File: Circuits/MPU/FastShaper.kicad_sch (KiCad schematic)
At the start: 34 parts, among them U20 ADA4805-2ARMZ, U21 ADA4805-2ARMZ

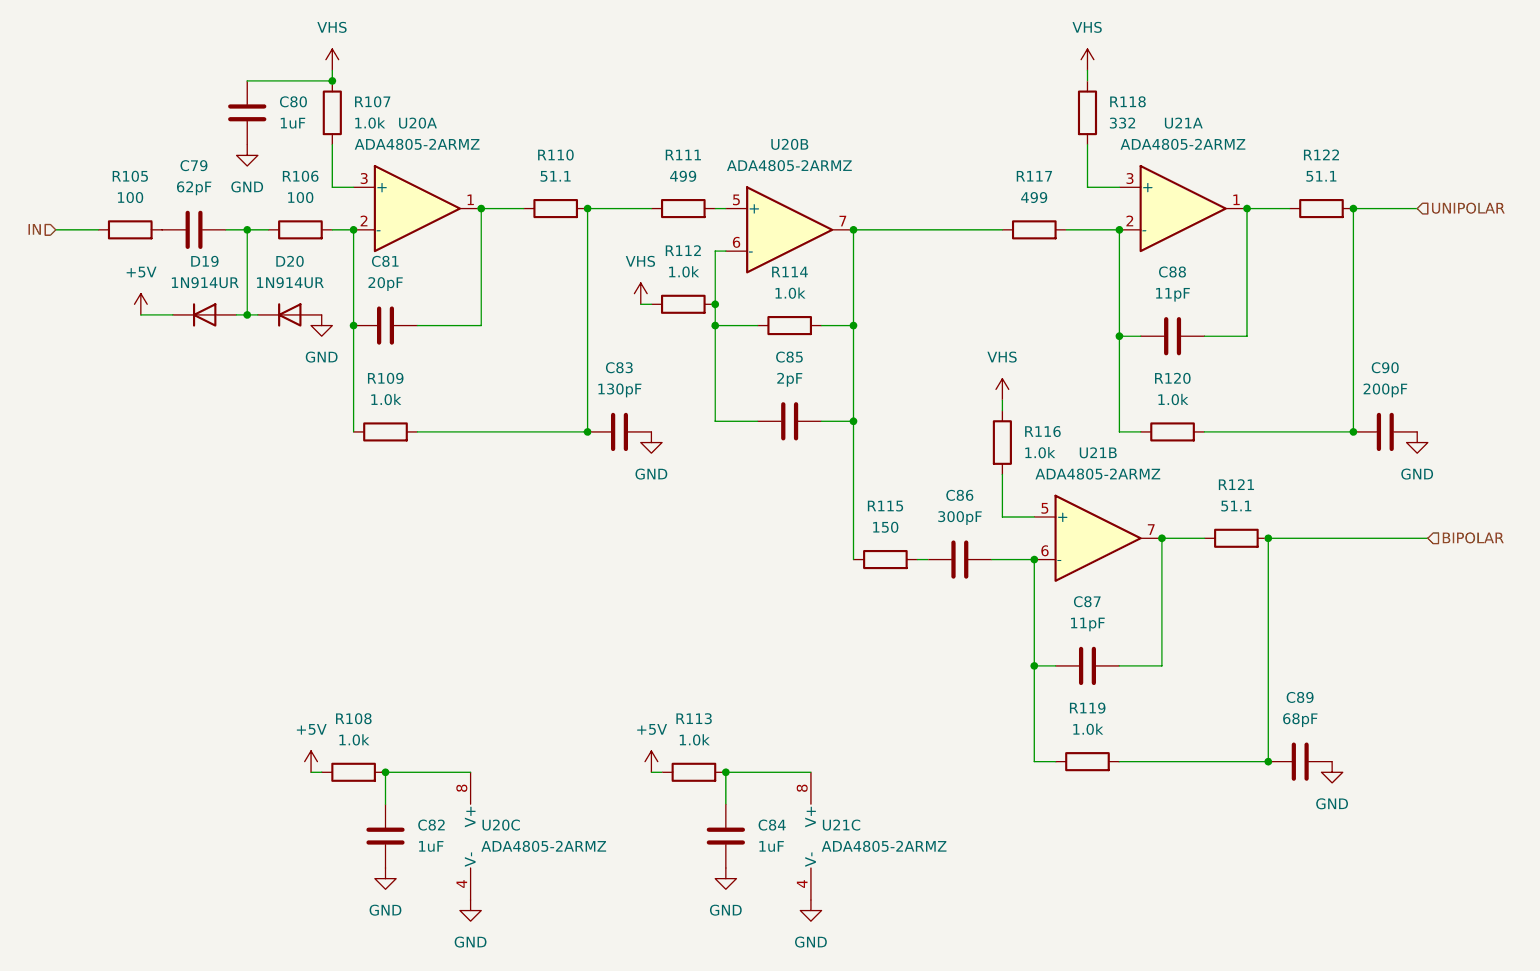
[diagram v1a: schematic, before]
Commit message: PPS is RS422, add MXINH
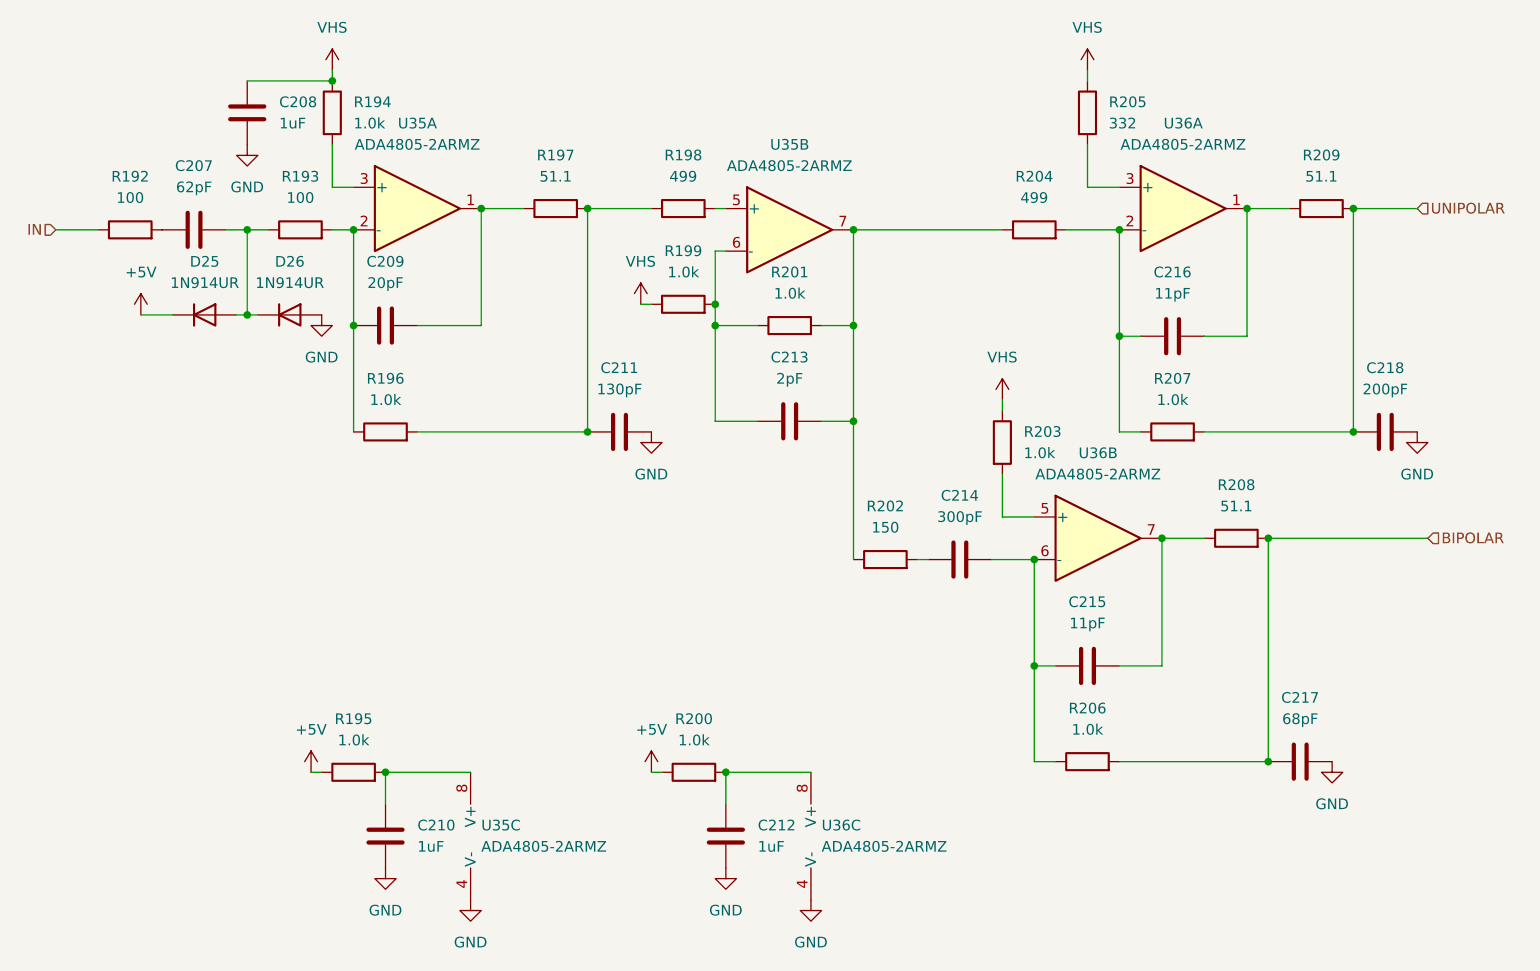
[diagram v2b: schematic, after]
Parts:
- renumbered C79 to C207, C80 to C208, C81 to C209, C82 to C210, C83 to C211, C84 to C212, C85 to C213, C86 to C214, C87 to C215, C88 to C216, C89 to C217, C90 to C218, D19 to D25, D20 to D26, R105 to R192, R106 to R193, R107 to R194, R108 to R195, R109 to R196, R110 to R197, R111 to R198, R112 to R199, R113 to R200, R114 to R201, R115 to R202, R116 to R203, R117 to R204, R118 to R205, R119 to R206, R120 to R207, R121 to R208, R122 to R209, U20 to U35, U21 to U36
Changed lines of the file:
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@@
 	(title_block
 		(title "QuERI MPU")
-		(date "2024-06-05")
-		(rev "RR1")
+		(date "2024-06-27")
+		(rev "RR3")
 		(company "Noqsi Aerospace Ltd")
 		(comment 1 "15 Blanchard Avenue, Billerica MA 01821")
@@
 		(dnp no)
 		(fields_autoplaced yes)
-		(property "Reference" "D20"
+		(property "Reference" "D26"
 			(at 69.85 72.39 0)
 			(effects
@@
 		(dnp no)
 		(fields_autoplaced yes)
-		(property "Reference" "U20"
+		(property "Reference" "U35"
 			(at 85.09 55.88 0)
 			(effects
@@
 		(dnp no)
 		(fields_autoplaced yes)
-		(property "Reference" "#PWR0191"
+		(property "Reference" "#PWR0309"
 			(at 132.08 154.94 0)
 			(effects
@@
 		(dnp no)
 		(fields_autoplaced yes)
-		(property "Reference" "#PWR0180"
+		(property "Reference" "#PWR0298"
 			(at 52.07 82.55 0)
 			(effects
@@
 		(dnp no)
 		(fields_autoplaced yes)
-		(property "Reference" "#PWR0192"
+		(property "Reference" "#PWR0310"
 			(at 154.94 92.71 0)
 			(effects
@@
 		(dnp no)
 		(fields_autoplaced yes)
-		(property "Reference" "#PWR0188"
+		(property "Reference" "#PWR0306"
 			(at 113.03 99.06 0)
 			(effects
@@
 		(dnp no)
 		(fields_autoplaced yes)
-		(property "Reference" "R117"
+		(property "Reference" "R204"
 			(at 158.75 62.23 90)
 			(effects
@@
 		(dnp no)
 		(fields_autoplaced yes)
-		(property "Reference" "#PWR0194"
+		(property "Reference" "#PWR0312"
 			(at 194.31 138.43 0)
 			(effects
@@
 		(dnp no)
 		(fields_autoplaced yes)
-		(property "Reference" "U20"
+		(property "Reference" "U35"
 			(at 92.71 139.7 0)
 			(effects
@@
 		(dnp no)
 		(fields_autoplaced yes)
-		(property "Reference" "U21"
+		(property "Reference" "U36"
 			(at 133.35 139.7 0)
 			(effects
@@
 		(dnp no)
 		(fields_autoplaced yes)
-		(property "Reference" "R120"
+		(property "Reference" "R207"
 			(at 175.26 86.36 90)
 			(effects
@@
 		(dnp no)
 		(fields_autoplaced yes)
-		(property "Reference" "C88"
+		(property "Reference" "C216"
 			(at 175.26 73.66 90)
 			(effects
@@
 		(dnp no)
 		(fields_autoplaced yes)
-		(property "Reference" "R118"
+		(property "Reference" "R205"
 			(at 167.64 53.34 0)
 			(effects
@@
 		(dnp no)
 		(fields_autoplaced yes)
-		(property "Reference" "D19"
+		(property "Reference" "D25"
 			(at 59.69 72.39 0)
 			(effects
@@
 		(dnp no)
 		(fields_autoplaced yes)
-		(property "Reference" "C84"
+		(property "Reference" "C212"
 			(at 125.73 139.7 0)
 			(effects
@@
 		(dnp no)
 		(fields_autoplaced yes)
-		(property "Reference" "R122"
+		(property "Reference" "R209"
 			(at 193.04 59.69 90)
 			(effects
@@
 		(dnp no)
 		(fields_autoplaced yes)
-		(property "Reference" "R111"
+		(property "Reference" "R198"
 			(at 116.84 59.69 90)
 			(effects
@@
 		(dnp no)
 		(fields_autoplaced yes)
-		(property "Reference" "U21"
+		(property "Reference" "U36"
 			(at 176.53 55.88 0)
 			(effects
@@
 		(dnp no)
 		(fields_autoplaced yes)
-		(property "Reference" "#PWR0185"
+		(property "Reference" "#PWR0303"
 			(at 81.28 151.13 0)
 			(effects
@@
 		(dnp no)
 		(fields_autoplaced yes)
-		(property "Reference" "R108"
+		(property "Reference" "R195"
 			(at 77.47 127 90)
 			(effects
@@
 		(dnp no)
 		(fields_autoplaced yes)
-		(property "Reference" "#PWR0181"
+		(property "Reference" "#PWR0299"
 			(at 64.77 64.77 0)
 			(effects
@@
 		(dnp no)
 		(fields_autoplaced yes)
-		(property "Reference" "C89"
+		(property "Reference" "C217"
 			(at 190.5 124.46 90)
 			(effects
@@
 		(dnp no)
 		(fields_autoplaced yes)
-		(property "Reference" "#PWR0182"
+		(property "Reference" "#PWR0300"
 			(at 72.39 137.16 0)
 			(effects
@@
 		(dnp no)
 		(fields_autoplaced yes)
-		(property "Reference" "R121"
+		(property "Reference" "R208"
 			(at 182.88 99.06 90)
 			(effects
@@
 		(dnp no)
 		(fields_autoplaced yes)
-		(property "Reference" "R116"
+		(property "Reference" "R203"
 			(at 157.48 92.71 0)
 			(effects
@@
 		(dnp no)
 		(fields_autoplaced yes)
-		(property "Reference" "C87"
+		(property "Reference" "C215"
 			(at 165.1 113.03 90)
 			(effects
@@
 		(dnp no)
 		(fields_autoplaced yes)
-		(property "Reference" "R106"
+		(property "Reference" "R193"
 			(at 71.12 62.23 90)
 			(effects
@@
 		(dnp no)
 		(fields_autoplaced yes)
-		(property "Reference" "R105"
+		(property "Reference" "R192"
 			(at 50.8 62.23 90)
 			(effects
@@
 		(dnp no)
 		(fields_autoplaced yes)
-		(property "Reference" "R109"
+		(property "Reference" "R196"
 			(at 81.28 86.36 90)
 			(effects
@@
 		(dnp no)
 		(fields_autoplaced yes)
-		(property "Reference" "C85"
+		(property "Reference" "C213"
 			(at 129.54 83.82 90)
 			(effects
@@
 		(dnp no)
 		(fields_autoplaced yes)
-		(property "Reference" "#PWR0189"
+		(property "Reference" "#PWR0307"
 			(at 113.03 137.16 0)
 			(effects
@@
 		(dnp no)
 		(fields_autoplaced yes)
-		(property "Reference" "U20"
+		(property "Reference" "U35"
 			(at 129.54 58.42 0)
 			(effects
@@
 		(dnp no)
 		(fields_autoplaced yes)
-		(property "Reference" "#PWR0195"
+		(property "Reference" "#PWR0313"
 			(at 204.47 99.06 0)
 			(effects
@@
 		(dnp no)
 		(fields_autoplaced yes)
-		(property "Reference" "R110"
+		(property "Reference" "R197"
 			(at 101.6 59.69 90)
 			(effects
@@
 		(dnp no)
 		(fields_autoplaced yes)
-		(property "Reference" "R114"
+		(property "Reference" "R201"
 			(at 129.54 73.66 90)
 			(effects
@@
 		(dnp no)
 		(fields_autoplaced yes)
-		(property "Reference" "R112"
+		(property "Reference" "R199"
 			(at 116.84 71.12 90)
 			(effects
@@
 		(dnp no)
 		(fields_autoplaced yes)
-		(property "Reference" "R119"
+		(property "Reference" "R206"
 			(at 165.1 125.73 90)
 			(effects
@@
 		(dnp no)
 		(fields_autoplaced yes)
-		(property "Reference" "R115"
+		(property "Reference" "R202"
 			(at 140.97 101.6 90)
 			(effects
@@
 		(dnp no)
 		(fields_autoplaced yes)
-		(property "Reference" "#PWR0187"
+		(property "Reference" "#PWR0305"
 			(at 111.76 81.28 0)
 			(effects
@@
 		(dnp no)
 		(fields_autoplaced yes)
-		(property "Reference" "C80"
+		(property "Reference" "C208"
 			(at 68.58 53.34 0)
 			(effects
@@
 		(dnp no)
 		(fields_autoplaced yes)
-		(property "Reference" "#PWR0190"
+		(property "Reference" "#PWR0308"
 			(at 121.92 151.13 0)
 			(effects
@@
 		(dnp no)
 		(fields_autoplaced yes)
-		(property "Reference" "C90"
+		(property "Reference" "C218"
 			(at 200.66 85.09 90)
 			(effects
@@
 		(dnp no)
 		(fields_autoplaced yes)
-		(property "Reference" "C86"
+		(property "Reference" "C214"
 			(at 149.86 100.33 90)
 			(effects
@@
 		(dnp no)
 		(fields_autoplaced yes)
-		(property "Reference" "U21"
+		(property "Reference" "U36"
 			(at 166.37 95.25 0)
 			(effects
@@
 		(dnp no)
 		(fields_autoplaced yes)
-		(property "Reference" "#PWR0183"
+		(property "Reference" "#PWR0301"
 			(at 73.66 85.09 0)
 			(effects
@@
 		(dnp no)
 		(fields_autoplaced yes)
-		(property "Reference" "#PWR0193"
+		(property "Reference" "#PWR0311"
 			(at 165.1 53.34 0)
 			(effects
@@
 		(dnp no)
 		(fields_autoplaced yes)
-		(property "Reference" "R107"
+		(property "Reference" "R194"
 			(at 77.47 53.34 0)
 			(effects
@@
 		(dnp no)
 		(fields_autoplaced yes)
-		(property "Reference" "C83"
+		(property "Reference" "C211"
 			(at 109.22 85.09 90)
 			(effects
@@
 		(dnp no)
 		(fields_autoplaced yes)
-		(property "Reference" "R113"
+		(property "Reference" "R200"
 			(at 118.11 127 90)
 			(effects
@@
 		(dnp no)
 		(fields_autoplaced yes)
-		(property "Reference" "C81"
+		(property "Reference" "C209"
 			(at 81.28 72.39 90)
 			(effects
@@
 		(dnp no)
 		(fields_autoplaced yes)
-		(property "Reference" "C79"
+		(property "Reference" "C207"
 			(at 58.42 60.96 90)
 			(effects
@@
 		(dnp no)
 		(fields_autoplaced yes)
-		(property "Reference" "#PWR0186"
+		(property "Reference" "#PWR0304"
 			(at 91.44 154.94 0)
 			(effects
@@
 		(dnp no)
 		(fields_autoplaced yes)
-		(property "Reference" "#PWR0184"
+		(property "Reference" "#PWR0302"
 			(at 74.93 53.34 0)
 			(effects
@@
 		(dnp no)
 		(fields_autoplaced yes)
-		(property "Reference" "C82"
+		(property "Reference" "C210"
 			(at 85.09 139.7 0)
 			(effects

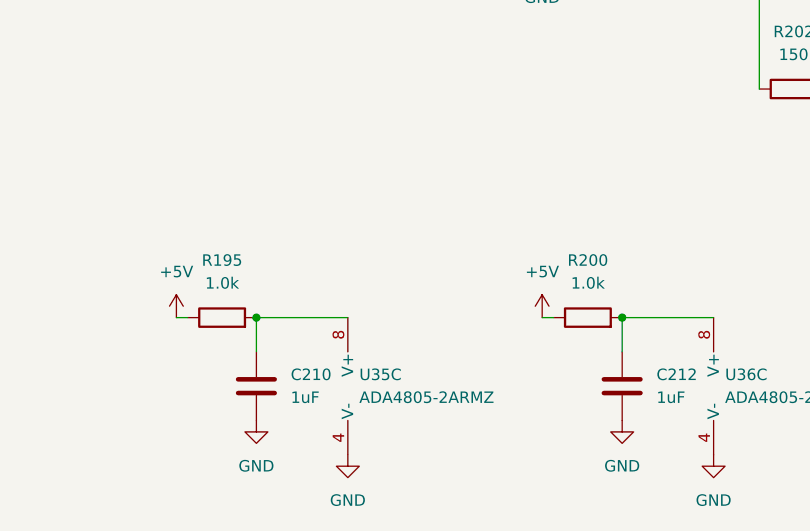
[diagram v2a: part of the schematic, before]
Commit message: Fix errors found by Norm Dobson
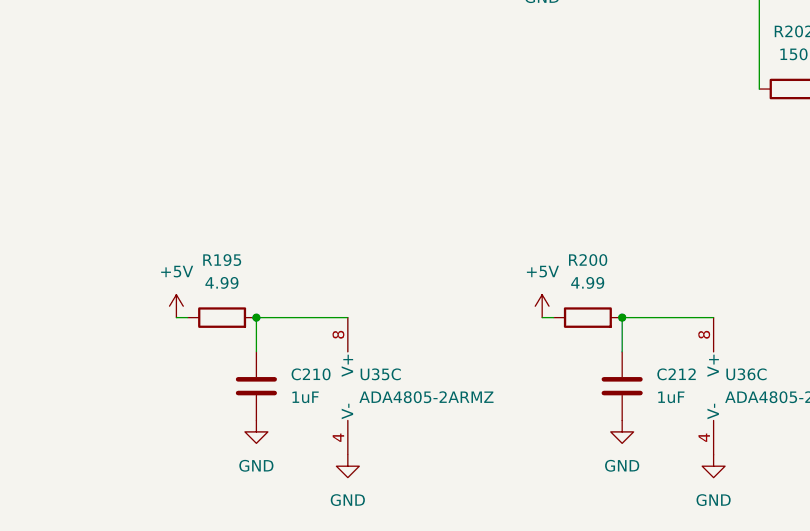
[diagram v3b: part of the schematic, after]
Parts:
- R195, R200: value 1.0k -> 4.99
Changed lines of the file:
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@@
 			)
 		)
-		(property "Value" "1.0k"
+		(property "Value" "4.99"
 			(at 77.47 129.54 90)
 			(effects
@@
 			)
 		)
-		(property "Value" "1.0k"
+		(property "Value" "4.99"
 			(at 118.11 129.54 90)
 			(effects
